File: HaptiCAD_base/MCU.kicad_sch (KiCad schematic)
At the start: 16 parts, among them J801 SWD, J802 Micro_SD_Card, U801 BMD-340-A-R, U802 ESD224DQA

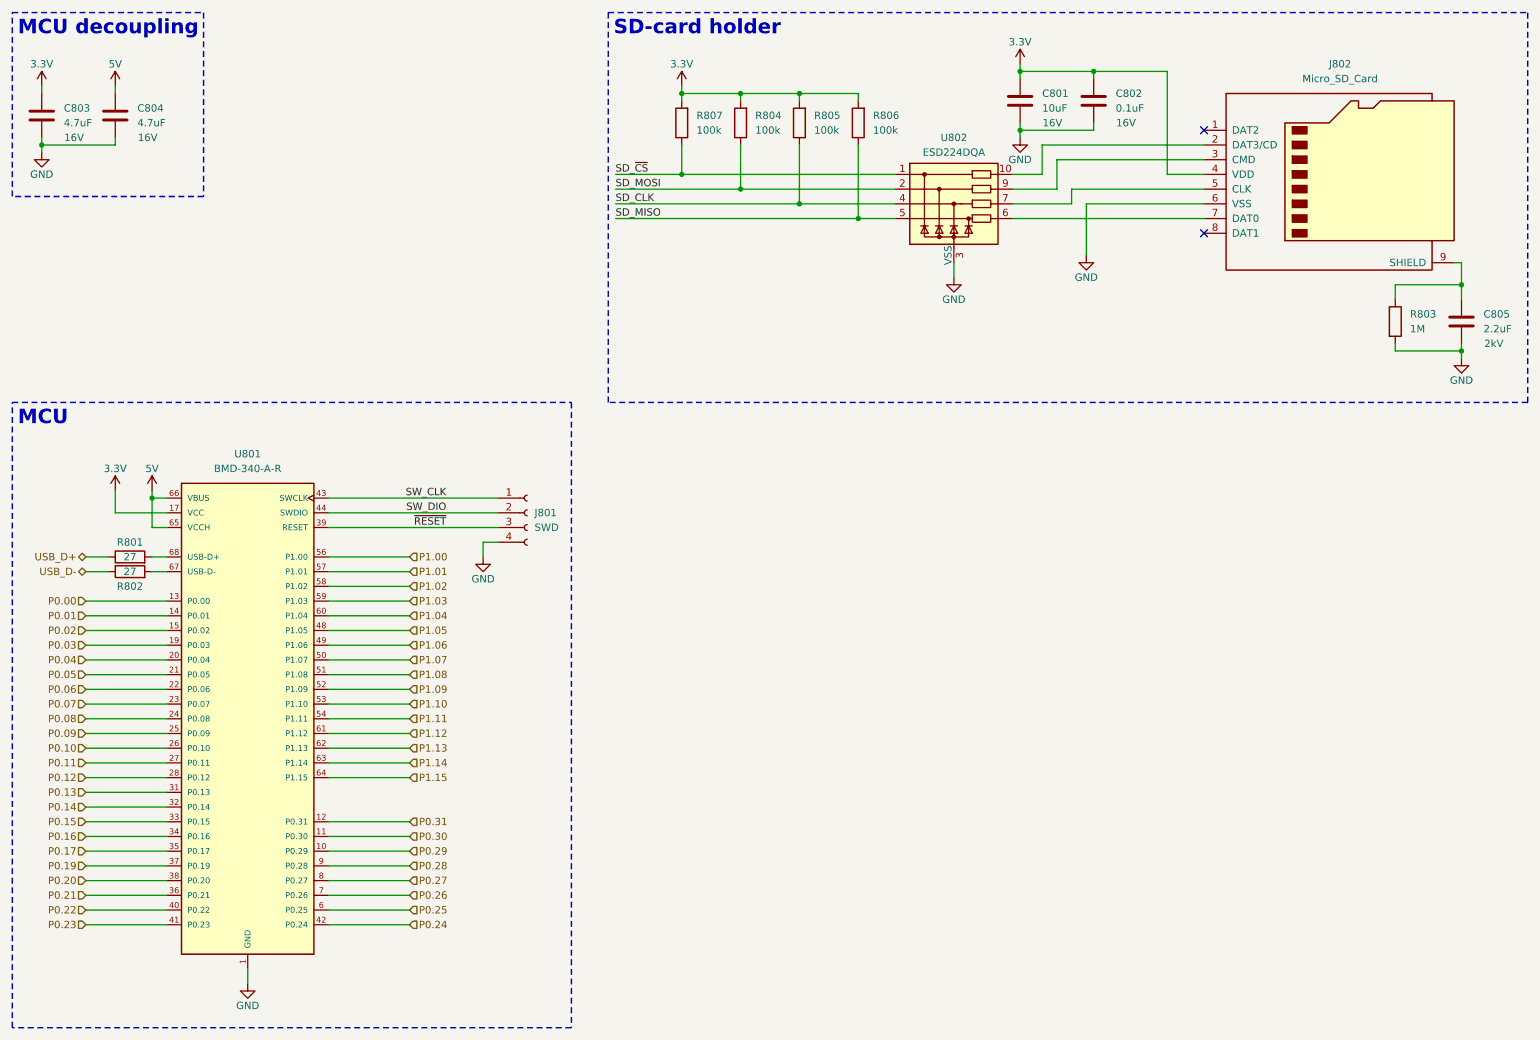
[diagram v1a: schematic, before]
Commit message: updated base schematic and PCB
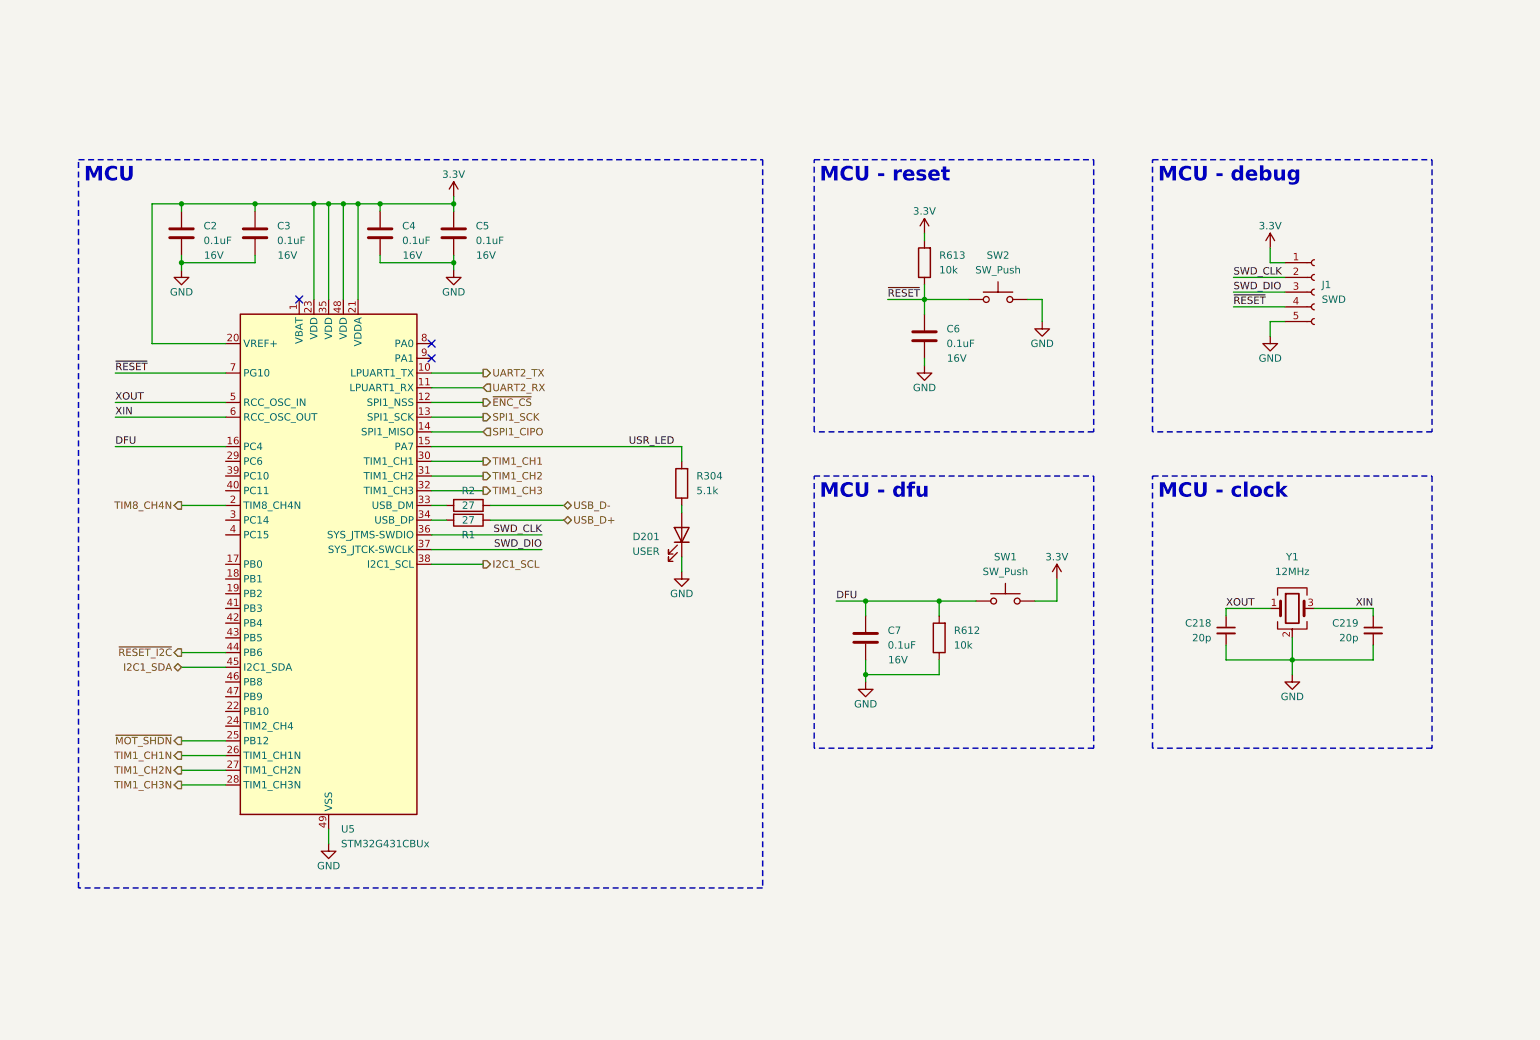
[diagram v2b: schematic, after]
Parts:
- removed C801: 10uF, Capacitor_SMD:C_0603_1608Metric, symbol Device:C
- removed C802: 0.1uF, Capacitor_SMD:C_0603_1608Metric, symbol Device:C
- removed C803, C804: 4.7uF, Capacitor_SMD:C_0603_1608Metric, symbol Device:C
- removed C805: 2.2uF, Capacitor_SMD:C_1206_3216Metric, symbol Device:C
- removed J801: SWD, Connector_PinSocket_2.54mm:PinSocket_1x04_P2.54mm_Vertical, symbol Connector:Conn_01x04_Socket
- removed J802: Micro_SD_Card, Connector_Card:microSD_HC_Wuerth_693072010801, symbol Connector:Micro_SD_Card
- removed R801, R802: 27, Resistor_SMD:R_0402_1005Metric, symbol Device:R
- removed R803: 1M, Resistor_SMD:R_1206_3216Metric, symbol Device:R
- removed R804, R805, R806, R807: 100k, Resistor_SMD:R_0402_1005Metric, symbol Device:R
- removed U801: BMD-340-A-R, BMD-340-A-R:RIGADO_BMD-340-A-R, symbol BMD-340-A-R:BMD-340-A-R
- removed U802: ESD224DQA, Package_DFN_QFN:Diodes_UDFN-10_1x2.5mm_P0.5mm, symbol Power_Protection:ESD224DQA
- added C2, C3, C4, C5, C6, C7: 0.1uF, Capacitor_SMD:C_0603_1608Metric, symbol Device:C
- added C218, C219: 20p, Capacitor_SMD:C_0402_1005Metric, symbol Device:C_Small
- added D201: USER, Diode_SMD:D_0603_1608Metric, symbol Device:LED
- added J1: SWD, symbol Connector:Conn_01x05_Socket
- added R1, R2: 27, Resistor_SMD:R_0402_1005Metric, symbol Device:R
- added R304: 5.1k, Resistor_SMD:R_0402_1005Metric, symbol Device:R
- added R612, R613: 10k, Resistor_SMD:R_0402_1005Metric, symbol Device:R
- added SW1, SW2: SW_Push, symbol Switch:SW_Push
- added U5: STM32G431CBUx, Package_DFN_QFN:QFN-48-1EP_7x7mm_P0.5mm_EP5.6x5.6mm, symbol MCU_ST_STM32G4:STM32G431CBUx
- added Y1: 12MHz, Crystal:Crystal_SMD_3225-4Pin_3.2x2.5mm, symbol Device:Crystal_GND24
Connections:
- net 3.3V: now also C2.1, C3.1, C4.1, C5.1, J1.1 (Pin_1), R613.2, SW1.2, U5.20 (VREF+), U5.21 (VDDA), U5.23 (VDD), U5.35 (VDD), U5.48 (VDD)
- net GND: now also C2.2, C218.2, C219.2, C3.2, C4.2, C5.2, C6.2, C7.2, D201.1 (K), J1.5 (Pin_5), R612.1, SW2.2, U5.49 (VSS), Y1.2 (G), Y1.4 (G)
- net USB_D+: now also R1.1
- net USB_D-: now also R2.1
- net ~{RESET}: now also C6.1, J1.4 (Pin_4), R613.1, SW2.1, U5.7 (PG10)
- new net: R2.2, U5.33 (PA11)
- new net: R1.2, U5.34 (PA12)
- new net: D201.2 (A), R304.1
- new net DFU: C7.1, R612.2, SW1.1, U5.16 (PC4)
- new net I2C1_SCL: U5.38 (PA15)
- new net I2C1_SDA: U5.45 (PB7)
- new net SPI1_CIPO: U5.14 (PA6)
- new net SPI1_SCK: U5.13 (PA5)
- new net SWD_CLK: J1.2 (Pin_2), U5.36 (PA13)
- new net SWD_DIO: J1.3 (Pin_3), U5.37 (PA14)
- new net TIM1_CH1: U5.30 (PA8)
- new net TIM1_CH1N: U5.26 (PB13)
- new net TIM1_CH2: U5.31 (PA9)
- new net TIM1_CH2N: U5.27 (PB14)
- new net TIM1_CH3: U5.32 (PA10)
- new net TIM1_CH3N: U5.28 (PB15)
- new net TIM8_CH4N: U5.2 (PC13)
- new net UART2_RX: U5.11 (PA3)
- new net UART2_TX: U5.10 (PA2)
- new net USR_LED: R304.2, U5.15 (PA7)
- new net XIN: C219.1, U5.6 (PF1), Y1.3
- new net XOUT: C218.1, U5.5 (PF0), Y1.1
- new net ~{ENC_CS}: U5.12 (PA4)
- new net ~{MOT_SHDN}: U5.25 (PB12)
- new net ~{RESET_I2C}: U5.44 (PB6)
- no-connect marks 2 -> 3

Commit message: Finished schematic of the base board
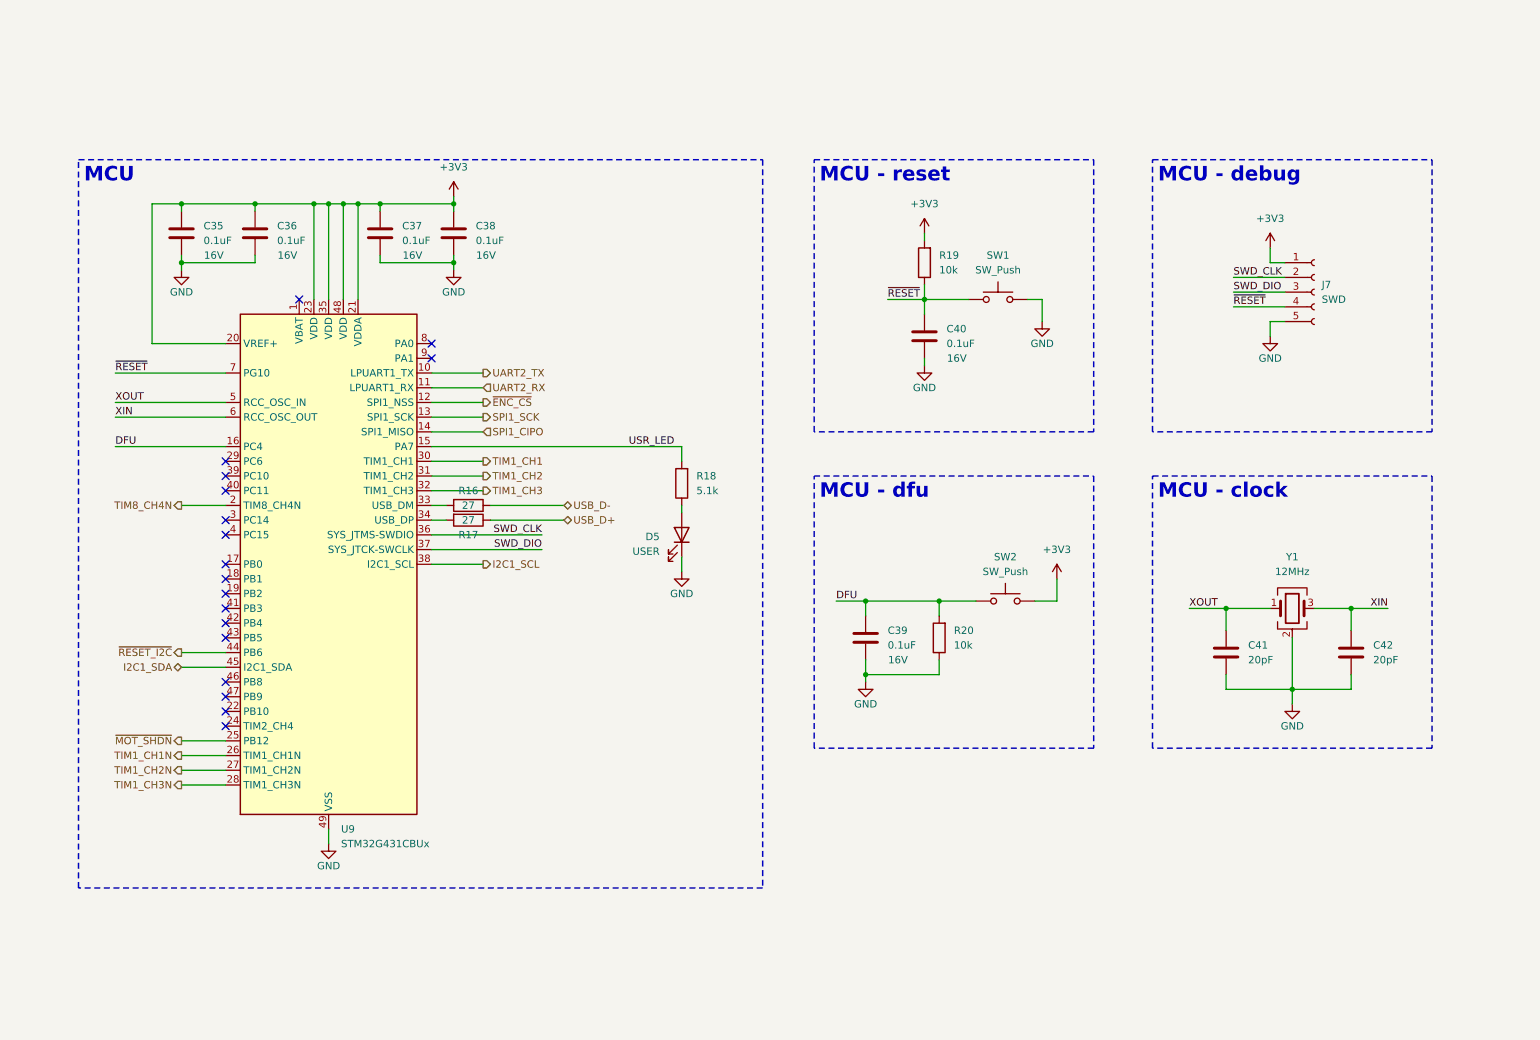
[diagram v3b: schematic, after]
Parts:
- removed C218, C219: 20p, Capacitor_SMD:C_0402_1005Metric, symbol Device:C_Small
- added C41, C42: 20pF, Capacitor_SMD:C_0402_1005Metric, symbol Device:C
- renumbered C2 to C35, C3 to C36, C4 to C37, C5 to C38, C7 to C39, C6 to C40, D201 to D5, J1 to J7, R2 to R16, R1 to R17, R304 to R18, R613 to R19, R612 to R20, SW2 to SW1, SW1 to SW2, U5 to U9
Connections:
- net GND: now also C41.2, C42.2
- net XIN: now also C42.1
- net XOUT: now also C41.1
- net 3.3V renamed +3V3
- no-connect marks 3 -> 18

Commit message: Finished the layout for the base and motor mount
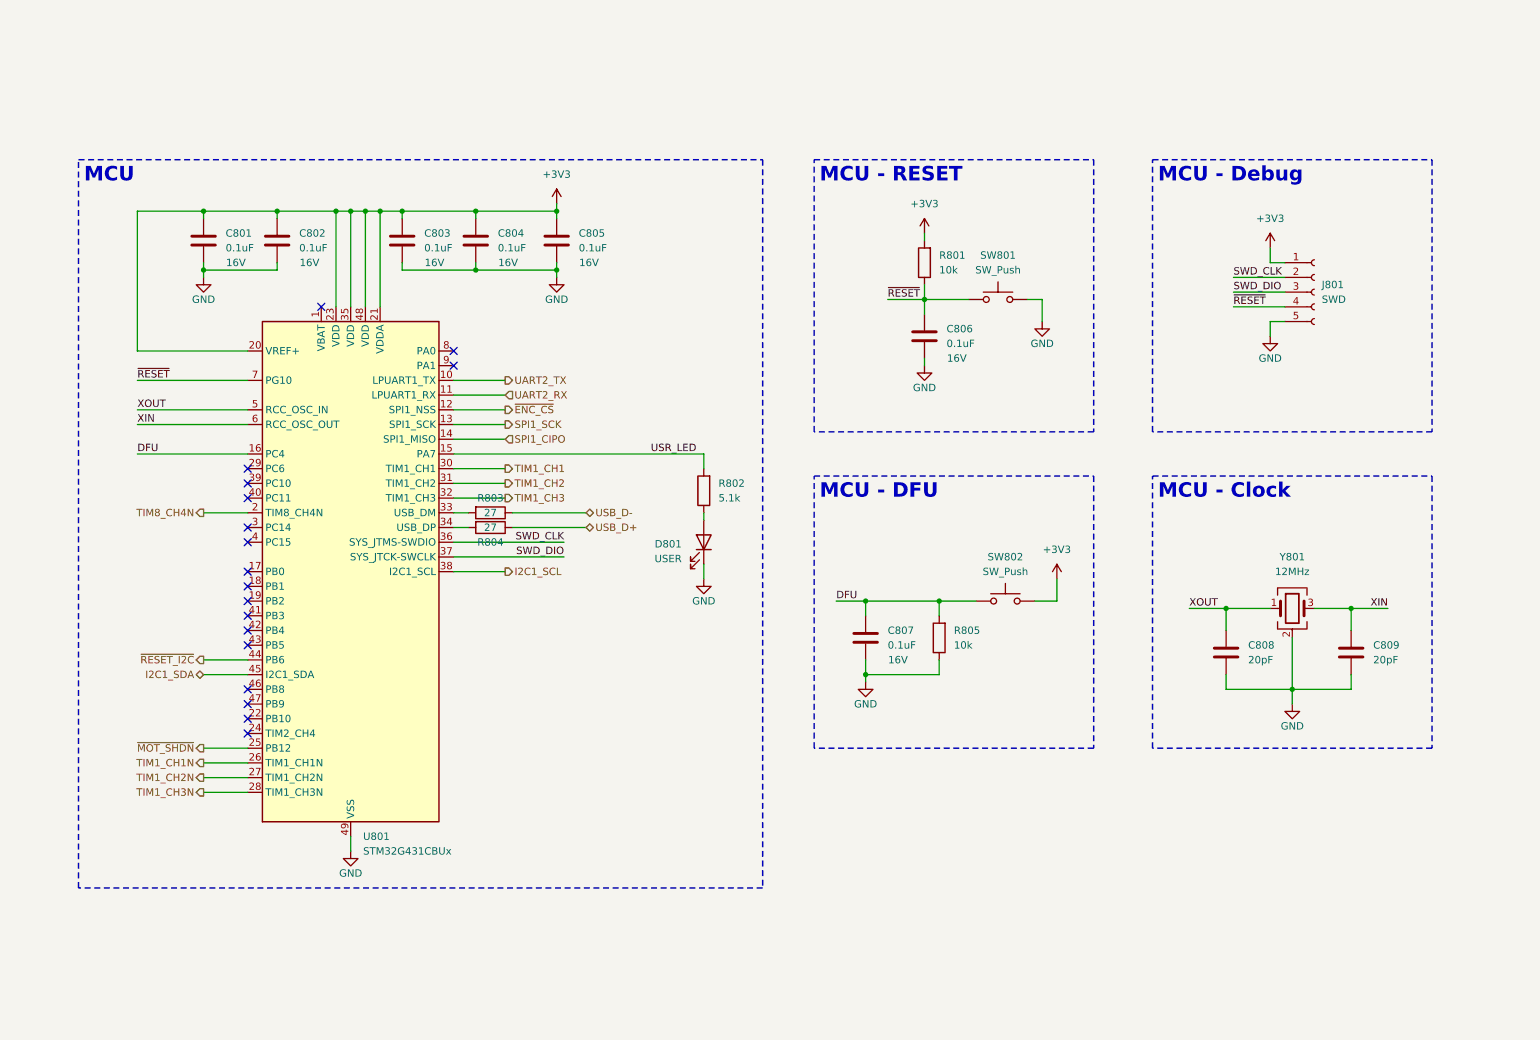
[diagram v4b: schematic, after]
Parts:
- added C805: 0.1uF, Capacitor_SMD:C_0402_1005Metric, symbol Device:C
- C801: renamed from C35; footprint Capacitor_SMD:C_0603_1608Metric -> Capacitor_SMD:C_0402_1005Metric
- C802: renamed from C36; footprint Capacitor_SMD:C_0603_1608Metric -> Capacitor_SMD:C_0402_1005Metric
- C803: renamed from C37; footprint Capacitor_SMD:C_0603_1608Metric -> Capacitor_SMD:C_0402_1005Metric
- C804: renamed from C38; footprint Capacitor_SMD:C_0603_1608Metric -> Capacitor_SMD:C_0402_1005Metric
- C806: renamed from C40; footprint Capacitor_SMD:C_0603_1608Metric -> Capacitor_SMD:C_0402_1005Metric
- C807: renamed from C39; footprint Capacitor_SMD:C_0603_1608Metric -> Capacitor_SMD:C_0402_1005Metric
- J801: renamed from J7; footprint (none) -> Connector_PinHeader_2.54mm:PinHeader_1x05_P2.54mm_Vertical_SMD_Pin1Left
- SW801: renamed from SW1; footprint (none) -> Button_Switch_SMD:SW_SPST_PTS810
- SW802: renamed from SW2; footprint (none) -> Button_Switch_SMD:SW_SPST_PTS810
- renumbered C41 to C808, C42 to C809, D5 to D801, R19 to R801, R18 to R802, R16 to R803, R17 to R804, R20 to R805, U9 to U801, Y1 to Y801
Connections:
- net +3V3: now also C805.1
- net GND: now also C805.2
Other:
- moved on the sheet: C801, C802, C803, C804, D801, R802, R803, R804, U801
